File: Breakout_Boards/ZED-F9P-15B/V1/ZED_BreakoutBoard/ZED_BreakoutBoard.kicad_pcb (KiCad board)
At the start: 2 copper layers, 23 x 37 mm, 15 parts, among them IC1 ZED-F9P-15B, J1 142-0701-801, J2 GPS_Conn_02x04_Top_Bottom

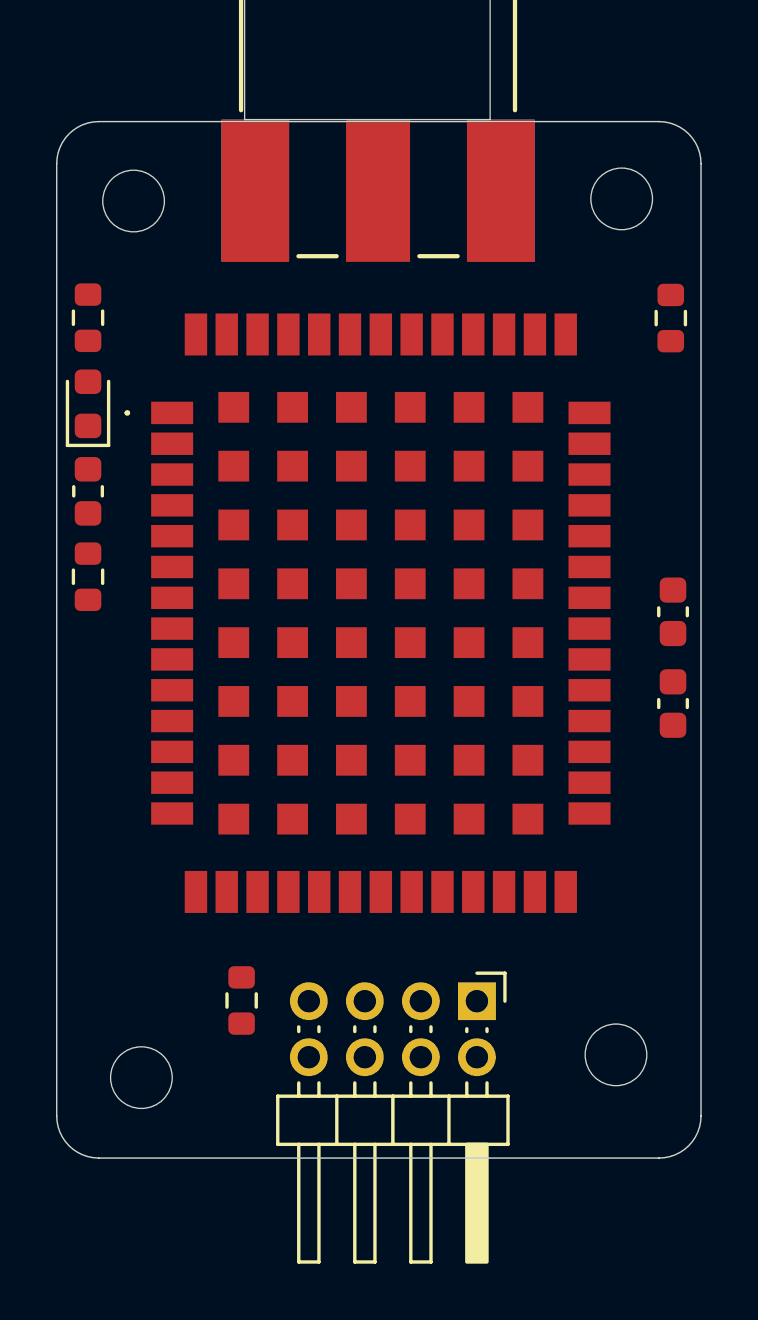
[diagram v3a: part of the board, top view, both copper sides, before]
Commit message: WIP : finition layout, fix connecteur GPS, passage 4 couches -> 6 couches
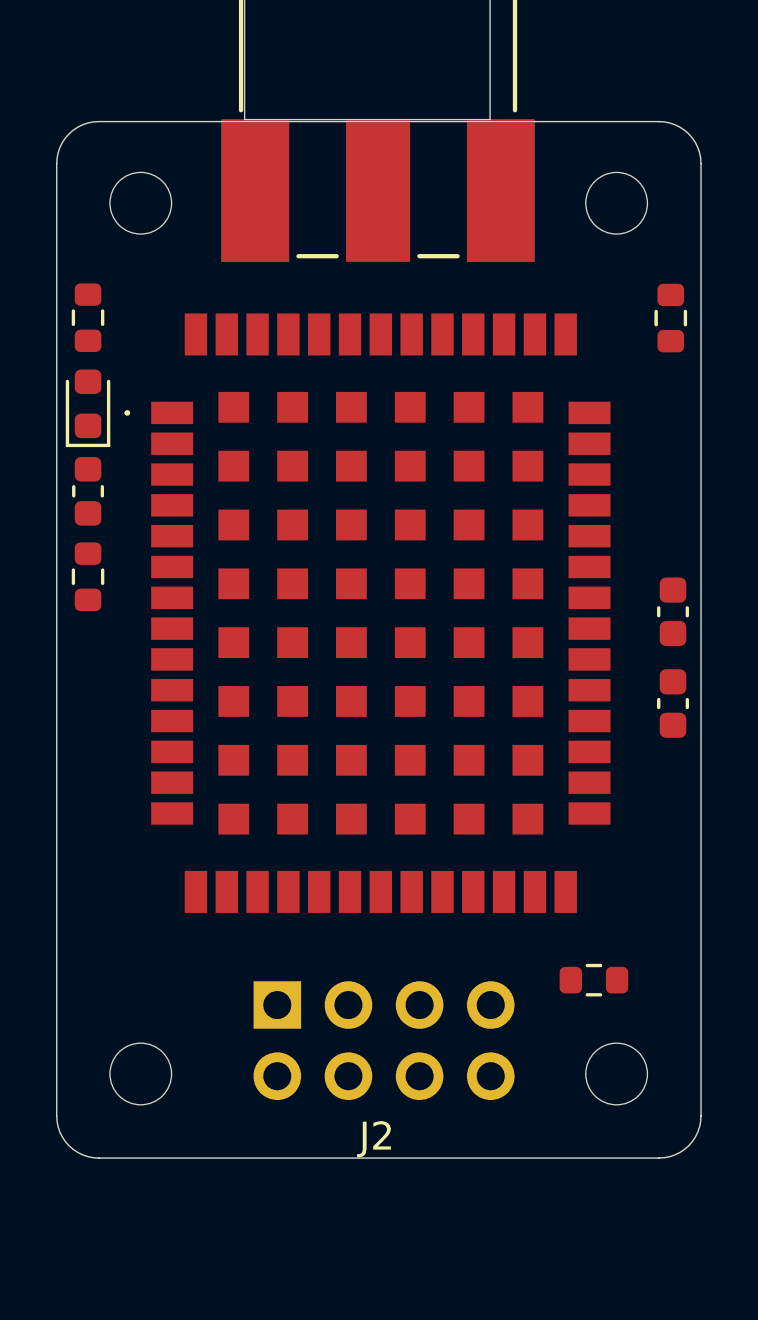
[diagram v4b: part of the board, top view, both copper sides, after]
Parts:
- J2: footprint Connector_PinHeader_2.00mm:PinHeader_2x04_P2.00mm_Horizontal -> Connector_PinHeader_2.54mm:PinHeader_2x04_P2.54mm_Vertical; moved to B.Cu
- moved ZED_R4 12.6 mm to (19.2, 36.4), turned to 180 degrees
- moved J2 7.13 mm to (7.87, 37.3)
- moved H4 0.68 mm to (20.0, 39.8)
- moved H1 0.27 mm to (3.00, 8.71)
- moved H2 0.24 mm to (20.0, 8.71)
- moved H3 0.13 mm to (3.00, 39.8)

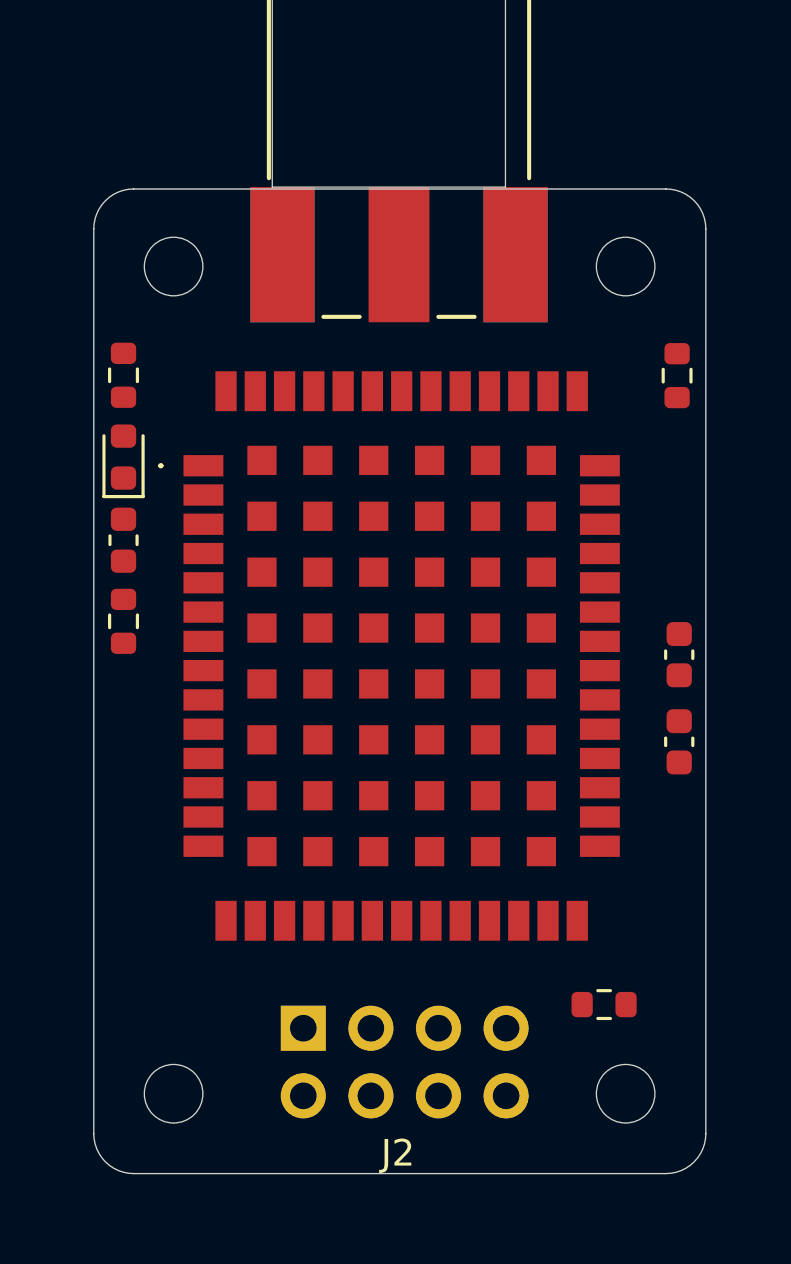
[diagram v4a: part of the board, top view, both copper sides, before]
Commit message: wip (breakoutboard) : add layered planes + tuning
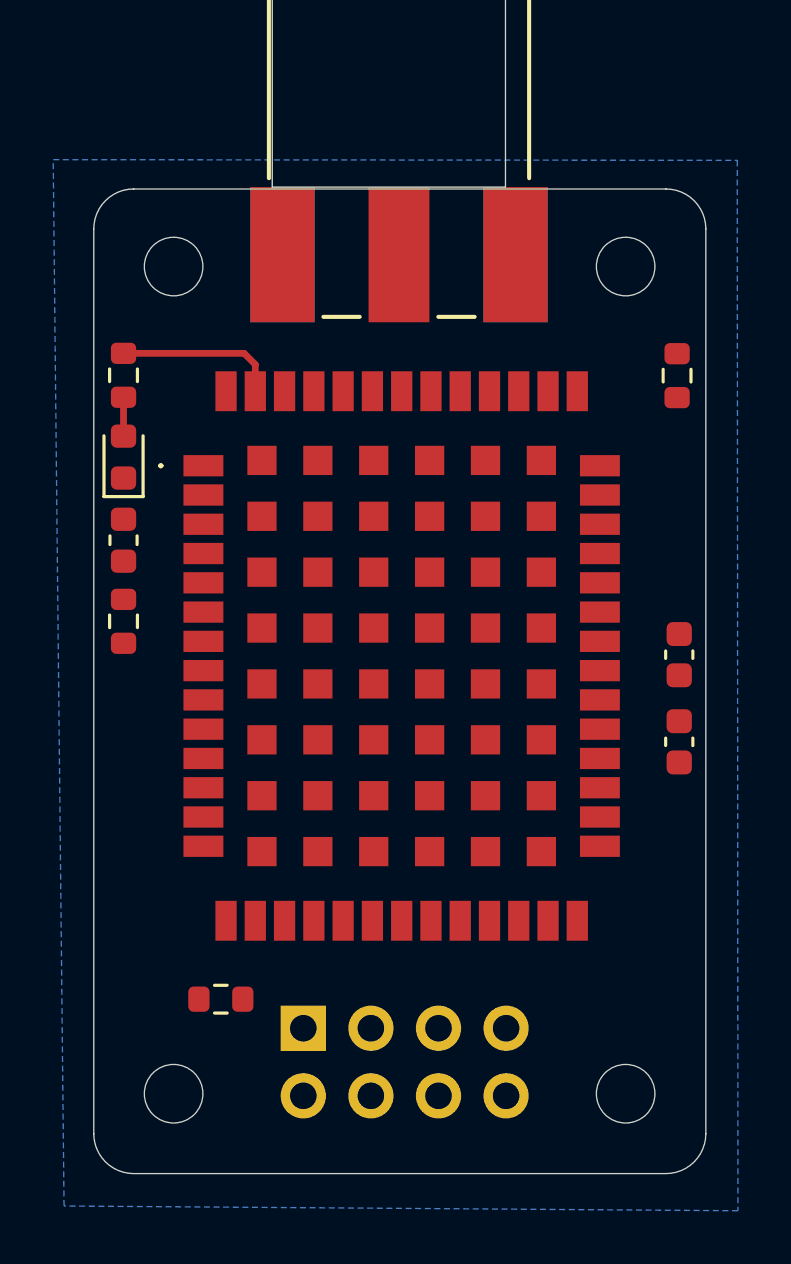
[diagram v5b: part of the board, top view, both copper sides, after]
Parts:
- moved ZED_R4 14.4 mm to (4.78, 36.2)
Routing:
- net Net-(IC1-TIMEPULSE): track 0.00 -> 6.13 mm
- net Net-(ZED_LED1-A): track 0.00 -> 1.46 mm
- added copper zone on B.Cu, net GPS_GND
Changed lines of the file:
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@@
 	(paper "A4")
 	(layers
-		(0 "F.Cu" signal)
-		(2 "B.Cu" signal)
+		(0 "F.Cu" signal "Signal")
+		(2 "B.Cu" power "GND")
 		(9 "F.Adhes" user "F.Adhesive")
 		(11 "B.Adhes" user "B.Adhesive")
@@
 	)
 	(setup
+		(stackup
+			(layer "F.SilkS"
+				(type "Top Silk Screen")
+			)
+			(layer "F.Paste"
+				(type "Top Solder Paste")
+			)
+			(layer "F.Mask"
+				(type "Top Solder Mask")
+				(thickness 0.01)
+			)
+			(layer "F.Cu"
+				(type "copper")
+				(thickness 0.035)
+			)
+			(layer "dielectric 1"
+				(type "core")
+				(thickness 1.51)
+				(material "FR4")
+				(epsilon_r 4.5)
+				(loss_tangent 0.02)
+			)
+			(layer "B.Cu"
+				(type "copper")
+				(thickness 0.035)
+			)
+			(layer "B.Mask"
+				(type "Bottom Solder Mask")
+				(thickness 0.01)
+			)
+			(layer "B.Paste"
+				(type "Bottom Solder Paste")
+			)
+			(layer "B.SilkS"
+				(type "Bottom Silk Screen")
+			)
+			(copper_finish "None")
+			(dielectric_constraints no)
+		)
 		(pad_to_mask_clearance 0)
 		(allow_soldermask_bridges_in_footprints no)
@@
 	(footprint "Resistor_SMD:R_0603_1608Metric"
 		(layer "F.Cu")
-		(at 19.177 36.449 180)
+		(at 4.7752 36.2458 180)
 		(descr "Resistor SMD 0603 (1608 Metric), square (rectangular) end terminal, IPC-7351 nominal, (Body size source: IPC-SM-782 page 72, https://www.pcb-3d.com/wordpress/wp-content/uploads/ipc-sm-782a_amendment_1_and_2.pdf), generated with kicad-footprint-generator")
 		(tags "resistor")
@@
 			(at 4.699 -3.556 0)
 			(layer "F.SilkS")
+			(hide yes)
 			(effects
 				(font
@@
 		(layer "Edge.Cuts")
 	)
+	(segment
+		(start 6.07 13.4)
+		(end 6.07 12.396)
+		(width 0.254)
+		(layer "F.Cu")
+		(net 3)
+	)
+	(segment
+		(start 5.6506 11.9766)
+		(end 1.1176 11.9766)
+		(width 0.254)
+		(layer "F.Cu")
+		(net 3)
+	)
+	(segment
+		(start 6.07 12.396)
+		(end 5.6506 11.9766)
+		(width 0.254)
+		(layer "F.Cu")
+		(net 3)
+	)
+	(segment
+		(start 1.1176 13.6266)
+		(end 1.1176 15.0875)
+		(width 0.254)
+		(layer "F.Cu")
+		(net 46)
+	)
+	(zone
+		(net 2)
+		(net_name "GPS_GND")
+		(layer "B.Cu")
+		(hatch edge 0.5)
+		(connect_pads
+			(clearance 0.5)
+		)
+		(min_thickness 0.25)
+		(filled_areas_thickness no)
+		(fill yes
+			(thermal_gap 0.5)
+			(thermal_bridge_width 0.5)
+		)
+		(polygon
+			(pts
+				(xy -1.524 4.699) (xy 24.1808 4.7244) (xy 24.2062 44.196) (xy -1.1176 44.0182)
+			)
+		)
+	)
 	(embedded_fonts no)

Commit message: wip (breakout): routing
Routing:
- net GPS_GND: track 0.00 -> 179.5 mm
- net ZED_EXTINT: track 0.00 -> 39.5 mm, vias 0 -> 2
- net ZED_TX_READY: track 0.00 -> 34.6 mm, vias 0 -> 2
- net GPS_USART6_RX: track 0.00 -> 32.6 mm, vias 0 -> 2
- net GPS_USART6_TX: track 0.00 -> 30.6 mm, vias 0 -> 2
- net GPS_VCC: track 0.00 -> 24.9 mm
- net Net-(J2-Pin_8): track 0.00 -> 15.6 mm
- net Net-(IC1-TIMEPULSE): track 6.13 -> 0.71 mm
- added copper zone on F.Cu, net GPS_GND
